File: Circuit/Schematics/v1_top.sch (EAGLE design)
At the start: 42 parts, among them IC1 LM2936MP-3.3, X2 16 Mhz, X3 16 Mhz

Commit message: Teensy board designed, redesigning system components board and making hardware components consistent
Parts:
- removed JP1: (no value), SparkFun-Connectors:M07
- added C10, C11, C12, C13, C14, C15, C16, C17, C18, C19, C20, C38, C39, C4, C40, C5, C6, C7, C8, C9: (no value), SparkFun-Capacitors:CAP0603-CAP
- added JP7: (no value), SparkFun-Connectors:M09
- added R1, R10, R11, R12, R13, R2, R5, R6: (no value), SparkFun-Resistors:RESISTOR0603-RES
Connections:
- new net SCL: JP7.9
- new net SDA: JP7.8
- net CE: now also JP7.3; no longer JP1.3
- net CSN: now also JP7.4; no longer JP1.4
- net MISO: now also JP7.6; no longer JP1.6
- net MOSI: now also JP7.5; no longer JP1.5
- net RX_W: now also JP7.1; no longer JP1.1
- net SCK: now also JP7.7; no longer JP1.7
- net TX_W: now also JP7.2; no longer JP1.2
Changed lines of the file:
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@@
 <part name="JP4" library="SparkFun-Connectors" deviceset="M02" device="LOCK"/>
 <part name="JP5" library="SparkFun-Connectors" deviceset="M02" device="LOCK"/>
-<part name="JP1" library="SparkFun-Connectors" deviceset="M07" device=""/>
 <part name="X3" library="crystals" deviceset="TXC-8Y" device="" value="16 Mhz"/>
 <part name="X2" library="crystals" deviceset="TXC-8Y" device="" value="16 Mhz"/>
 <part name="C1" library="SparkFun-Capacitors" deviceset="CAP" device="0402-CAP" value="1 uF"/>
 <part name="JP6" library="SparkFun-Connectors" deviceset="M02" device="LOCK"/>
+<part name="R1" library="SparkFun-Resistors" deviceset="RESISTOR" device="0603-RES"/>
+<part name="R2" library="SparkFun-Resistors" deviceset="RESISTOR" device="0603-RES"/>
+<part name="R5" library="SparkFun-Resistors" deviceset="RESISTOR" device="0603-RES"/>
+<part name="R6" library="SparkFun-Resistors" deviceset="RESISTOR" device="0603-RES"/>
+<part name="R10" library="SparkFun-Resistors" deviceset="RESISTOR" device="0603-RES"/>
+<part name="R11" library="SparkFun-Resistors" deviceset="RESISTOR" device="0603-RES"/>
+<part name="R12" library="SparkFun-Resistors" deviceset="RESISTOR" device="0603-RES"/>
+<part name="R13" library="SparkFun-Resistors" deviceset="RESISTOR" device="0603-RES"/>
+<part name="C4" library="SparkFun-Capacitors" deviceset="CAP" device="0603-CAP"/>
+<part name="C5" library="SparkFun-Capacitors" deviceset="CAP" device="0603-CAP"/>
+<part name="C6" library="SparkFun-Capacitors" deviceset="CAP" device="0603-CAP"/>
+<part name="C7" library="SparkFun-Capacitors" deviceset="CAP" device="0603-CAP"/>
+<part name="C8" library="SparkFun-Capacitors" deviceset="CAP" device="0603-CAP"/>
+<part name="C9" library="SparkFun-Capacitors" deviceset="CAP" device="0603-CAP"/>
+<part name="C10" library="SparkFun-Capacitors" deviceset="CAP" device="0603-CAP"/>
+<part name="C11" library="SparkFun-Capacitors" deviceset="CAP" device="0603-CAP"/>
+<part name="C12" library="SparkFun-Capacitors" deviceset="CAP" device="0603-CAP"/>
+<part name="C13" library="SparkFun-Capacitors" deviceset="CAP" device="0603-CAP"/>
+<part name="C14" library="SparkFun-Capacitors" deviceset="CAP" device="0603-CAP"/>
+<part name="C15" library="SparkFun-Capacitors" deviceset="CAP" device="0603-CAP"/>
+<part name="C16" library="SparkFun-Capacitors" deviceset="CAP" device="0603-CAP"/>
+<part name="C17" library="SparkFun-Capacitors" deviceset="CAP" device="0603-CAP"/>
+<part name="C18" library="SparkFun-Capacitors" deviceset="CAP" device="0603-CAP"/>
+<part name="C19" library="SparkFun-Capacitors" deviceset="CAP" device="0603-CAP"/>
+<part name="C20" library="SparkFun-Capacitors" deviceset="CAP" device="0603-CAP"/>
+<part name="C38" library="SparkFun-Capacitors" deviceset="CAP" device="0603-CAP"/>
+<part name="C39" library="SparkFun-Capacitors" deviceset="CAP" device="0603-CAP"/>
+<part name="C40" library="SparkFun-Capacitors" deviceset="CAP" device="0603-CAP"/>
+<part name="JP7" library="SparkFun-Connectors" deviceset="M09" device=""/>
 </parts>
 <sheets>
@@
 <instance part="JP4" gate="G$1" x="193.04" y="129.54" rot="R180"/>
 <instance part="JP5" gate="G$1" x="208.28" y="129.54" rot="R180"/>
-<instance part="JP1" gate="G$1" x="231.14" y="132.08" rot="R180"/>
 <instance part="X3" gate="G$1" x="60.96" y="104.14" rot="R90"/>
 <instance part="X2" gate="G$1" x="137.16" y="12.7"/>
 <instance part="C1" gate="G$1" x="93.98" y="111.76"/>
 <instance part="JP6" gate="G$1" x="203.2" y="109.22" rot="R180"/>
+<instance part="R1" gate="G$1" x="20.32" y="99.06"/>
+<instance part="R2" gate="G$1" x="55.88" y="2.54"/>
+<instance part="R5" gate="G$1" x="96.52" y="22.86"/>
+<instance part="R6" gate="G$1" x="152.4" y="22.86"/>
+<instance part="R10" gate="G$1" x="144.78" y="86.36"/>
+<instance part="R11" gate="G$1" x="205.74" y="22.86"/>
+<instance part="R12" gate="G$1" x="205.74" y="15.24"/>
+<instance part="R13" gate="G$1" x="205.74" y="7.62"/>
+<instance part="C4" gate="G$1" x="-2.54" y="76.2"/>
+<instance part="C5" gate="G$1" x="76.2" y="142.24"/>
+<instance part="C6" gate="G$1" x="73.66" y="116.84"/>
+<instance part="C7" gate="G$1" x="78.74" y="91.44"/>
+<instance part="C8" gate="G$1" x="93.98" y="99.06"/>
+<instance part="C9" gate="G$1" x="101.6" y="99.06"/>
+<instance part="C10" gate="G$1" x="129.54" y="99.06"/>
+<instance part="C11" gate="G$1" x="116.84" y="86.36"/>
+<instance part="C12" gate="G$1" x="137.16" y="99.06"/>
+<instance part="C13" gate="G$1" x="144.78" y="99.06"/>
+<instance part="C14" gate="G$1" x="149.86" y="99.06"/>
+<instance part="C15" gate="G$1" x="154.94" y="99.06"/>
+<instance part="C16" gate="G$1" x="160.02" y="99.06"/>
+<instance part="C17" gate="G$1" x="165.1" y="99.06"/>
+<instance part="C18" gate="G$1" x="180.34" y="76.2"/>
+<instance part="C19" gate="G$1" x="198.12" y="55.88"/>
+<instance part="C20" gate="G$1" x="160.02" y="25.4"/>
+<instance part="C38" gate="G$1" x="170.18" y="25.4"/>
+<instance part="C39" gate="G$1" x="132.08" y="-7.62"/>
+<instance part="C40" gate="G$1" x="142.24" y="-7.62"/>
+<instance part="JP7" gate="G$1" x="236.22" y="99.06" rot="R180"/>
 </instances>
 <busses>
@@
 </segment>
 <segment>
-<pinref part="JP1" gate="G$1" pin="2"/>
-<wire x1="226.06" y1="134.62" x2="223.52" y2="134.62" width="0.1524" layer="91"/>
+<pinref part="JP7" gate="G$1" pin="2"/>
+<wire x1="226.06" y1="106.68" x2="223.52" y2="106.68" width="0.1524" layer="91"/>
 </segment>
 </net>
@@
 </segment>
 <segment>
-<pinref part="JP1" gate="G$1" pin="1"/>
-<wire x1="226.06" y1="137.16" x2="223.52" y2="137.16" width="0.1524" layer="91"/>
+<pinref part="JP7" gate="G$1" pin="1"/>
+<wire x1="226.06" y1="109.22" x2="223.52" y2="109.22" width="0.1524" layer="91"/>
 </segment>
 </net>
@@
 </segment>
 <segment>
-<pinref part="JP1" gate="G$1" pin="3"/>
-<wire x1="226.06" y1="132.08" x2="223.52" y2="132.08" width="0.1524" layer="91"/>
+<pinref part="JP7" gate="G$1" pin="3"/>
+<wire x1="226.06" y1="104.14" x2="223.52" y2="104.14" width="0.1524" layer="91"/>
 </segment>
 </net>
@@
 </segment>
 <segment>
-<pinref part="JP1" gate="G$1" pin="4"/>
-<wire x1="226.06" y1="129.54" x2="223.52" y2="129.54" width="0.1524" layer="91"/>
+<pinref part="JP7" gate="G$1" pin="4"/>
+<wire x1="226.06" y1="101.6" x2="223.52" y2="101.6" width="0.1524" layer="91"/>
 </segment>
 </net>
@@
 </segment>
 <segment>
-<pinref part="JP1" gate="G$1" pin="7"/>
-<wire x1="226.06" y1="121.92" x2="223.52" y2="121.92" width="0.1524" layer="91"/>
+<pinref part="JP7" gate="G$1" pin="7"/>
+<wire x1="226.06" y1="93.98" x2="223.52" y2="93.98" width="0.1524" layer="91"/>
 </segment>
 </net>
@@
 </segment>
 <segment>
-<pinref part="JP1" gate="G$1" pin="5"/>
-<wire x1="226.06" y1="127" x2="223.52" y2="127" width="0.1524" layer="91"/>
+<pinref part="JP7" gate="G$1" pin="5"/>
+<wire x1="226.06" y1="99.06" x2="223.52" y2="99.06" width="0.1524" layer="91"/>
 </segment>
 </net>
@@
 </segment>
 <segment>
-<pinref part="JP1" gate="G$1" pin="6"/>
-<wire x1="226.06" y1="124.46" x2="223.52" y2="124.46" width="0.1524" layer="91"/>
+<pinref part="JP7" gate="G$1" pin="6"/>
+<wire x1="226.06" y1="96.52" x2="223.52" y2="96.52" width="0.1524" layer="91"/>
 </segment>
 </net>
@@
 </segment>
 </net>
+<net name="SDA" class="0">
+<segment>
+<pinref part="JP7" gate="G$1" pin="8"/>
+<wire x1="226.06" y1="91.44" x2="223.52" y2="91.44" width="0.1524" layer="91"/>
+</segment>
+</net>
+<net name="SCL" class="0">
+<segment>
+<pinref part="JP7" gate="G$1" pin="9"/>
+<wire x1="226.06" y1="88.9" x2="223.52" y2="88.9" width="0.1524" layer="91"/>
+</segment>
+</net>

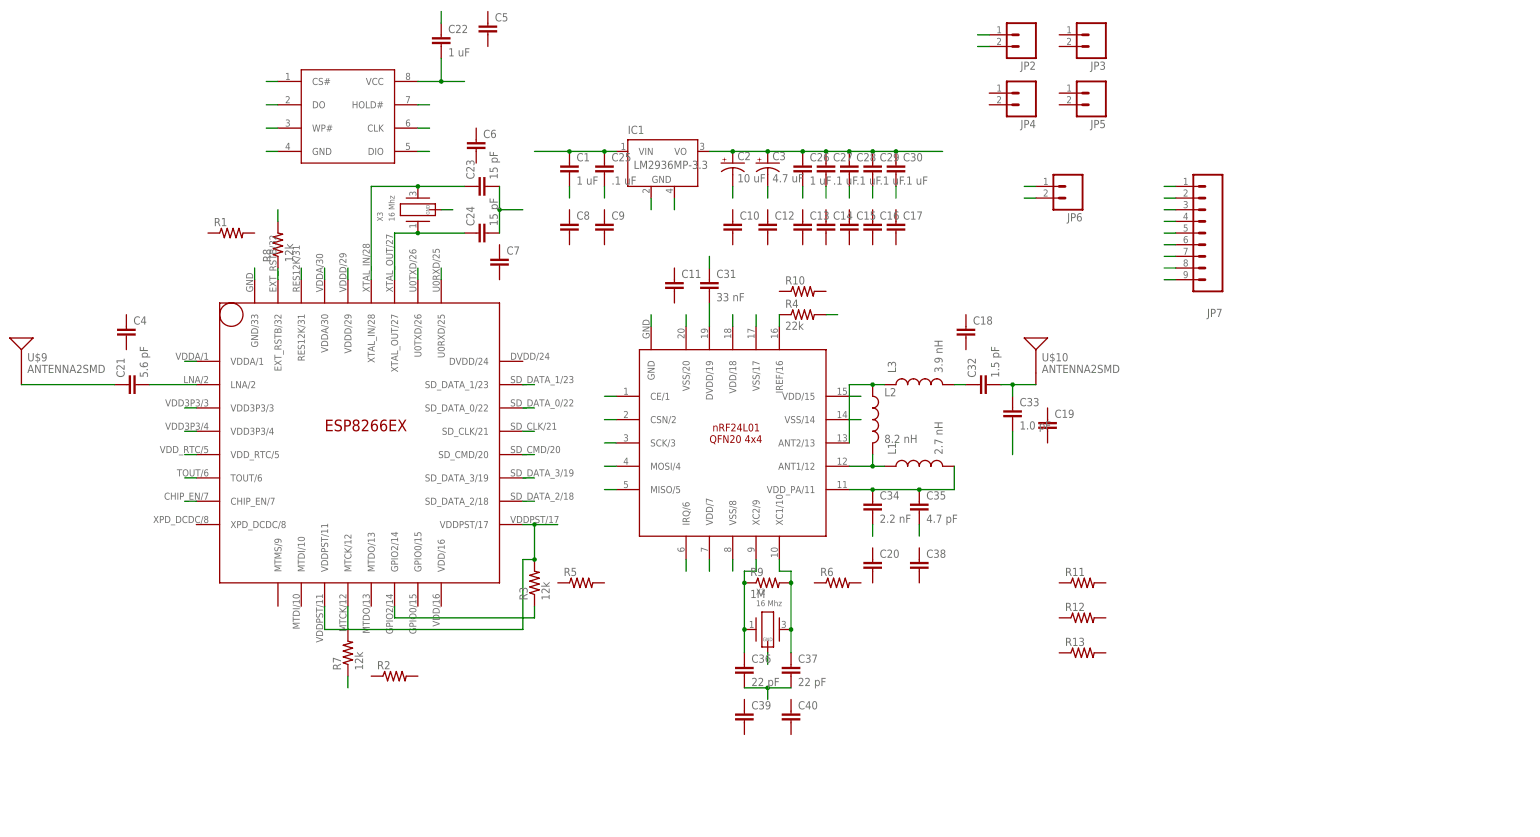
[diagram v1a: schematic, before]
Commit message: System components board almost done. Final tweaking
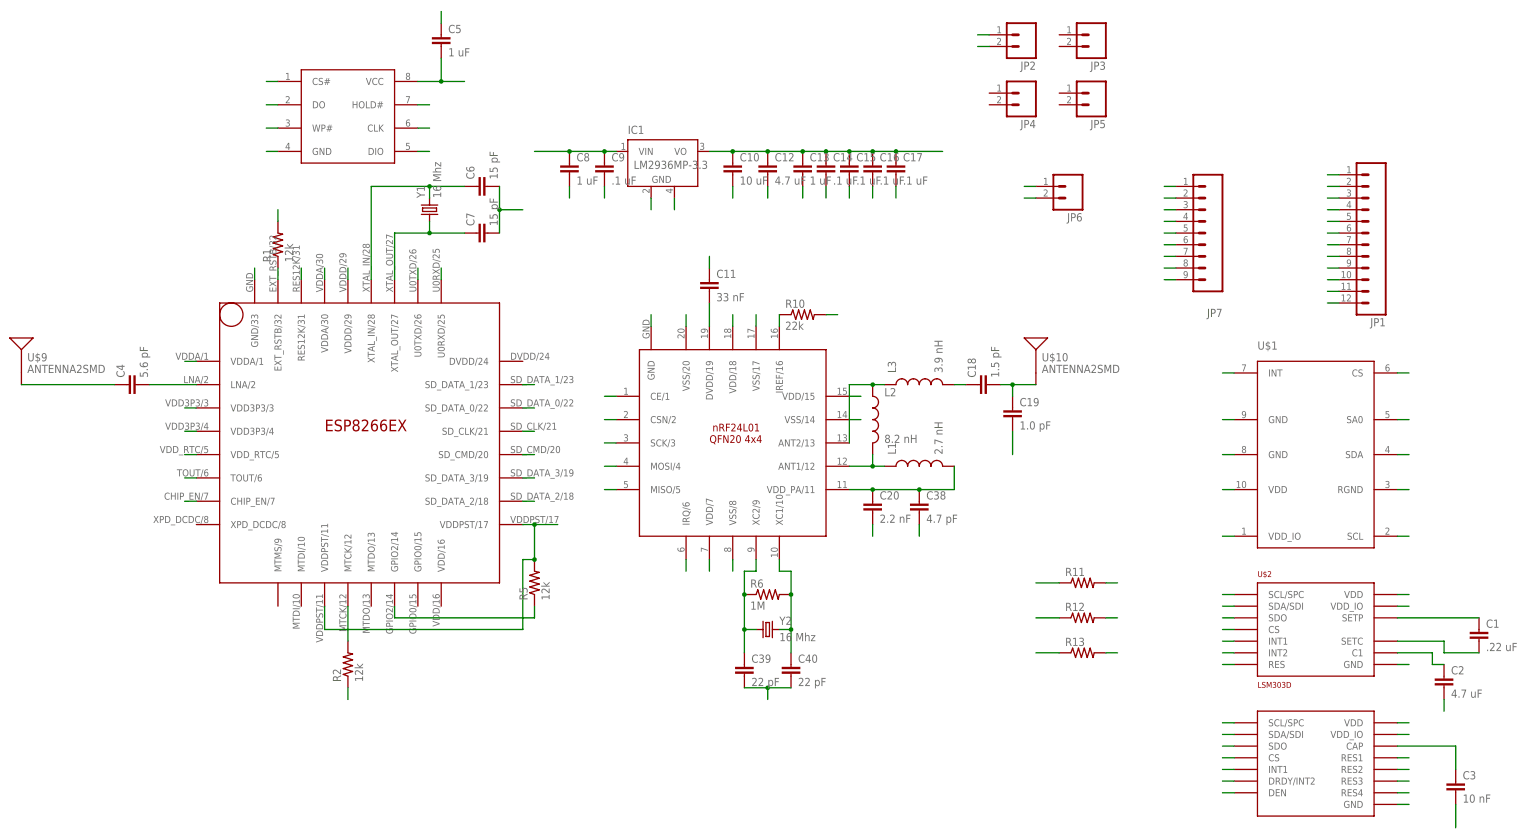
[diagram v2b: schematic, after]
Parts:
- removed C21: 5.6 pF, SparkFun-Capacitors:CAP0402-CAP
- removed C22, C26: 1 uF, SparkFun-Capacitors:CAP0402-CAP
- removed C23, C24: 15 pF, SparkFun-Capacitors:CAP0402-CAP
- removed C25, C27, C28, C29, C30: .1 uF, SparkFun-Capacitors:CAP0402-CAP
- removed C31: 33 nF, SparkFun-Capacitors:CAP0402-CAP
- removed C32: 1.5 pF, SparkFun-Capacitors:CAP0402-CAP
- removed C33: 1.0 pF, SparkFun-Capacitors:CAP0402-CAP
- removed C34: 2.2 nF, SparkFun-Capacitors:CAP0402-CAP
- removed C35: 4.7 pF, SparkFun-Capacitors:CAP0402-CAP
- removed C36, C37: 22 pF, SparkFun-Capacitors:CAP0402-CAP
- removed R3, R7, R8: 12k, SparkFun-Resistors:RESISTOR0402
- removed R4: 22k, SparkFun-Resistors:RESISTOR0402
- removed R9: 1M, SparkFun-Resistors:RESISTOR0402
- removed X2, X3: 16 Mhz, crystals:TXC-8Y
- added JP1: (no value), SparkFun-Connectors:M12PTH
- added U$1: LPS25H, chips:LPS25H
- added U$2: LSM303D, st:LSM303D
- added U$3: L3GD20H, st:L3GD20H
- added Y1, Y2: 16 Mhz, SparkFun-FreqCtrl:CRYSTAL5X3
- C1: value 1 uF -> .22 uF; device SparkFun-Capacitors:CAP0402-CAP -> SparkFun-Capacitors:CAP0603-CAP
- C10: value (none) -> 10 uF
- C11: value (none) -> 33 nF
- C12: value (none) -> 4.7 uF
- C13, C5, C8: value (none) -> 1 uF
- C14, C15, C16, C17, C9: value (none) -> .1 uF
- C18: value (none) -> 1.5 pF
- C19: value (none) -> 1.0 pF
- C2: value 10 uF -> 4.7 uF; device SparkFun-Capacitors:CAP_POL1206 -> SparkFun-Capacitors:CAP0603-CAP
- C20: value (none) -> 2.2 nF
- C3: value 4.7 uF -> 10 nF; device SparkFun-Capacitors:CAP_POL1206 -> SparkFun-Capacitors:CAP0603-CAP
- C38: value (none) -> 4.7 pF
- C39, C40: value (none) -> 22 pF
- C4: value (none) -> 5.6 pF
- C6, C7: value (none) -> 15 pF
- R1, R2, R5: value (none) -> 12k
- R10: value (none) -> 22k
- R6: value (none) -> 1M
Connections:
- removed net N$12: R7.2, WIFI.MTCK/12
- new net N$14: U$1.INT
- new net N$3: R2.2, WIFI.MTCK/12
- new net N$35: U$2.INT1
- new net N$36: U$2.INT2
- new net N$42: C1.2, U$2.SETC
- new net N$43: C2.1, U$2.C1
- new net N$49: U$3.INT1
- new net N$50: U$3.DRDY/INT2
- new net N$54: C3.1, U$3.CAP
- new net N$58: U$3.RES4
- new net SDO: R13.2, U$1.SA0, U$2.SDO, U$3.SDO
- new net SETP: C1.1, U$2.SETP
- net GND: now also C10.2, C11.1, C12.2, C13.2, C14.2, C15.2, C16.2, C17.2, C19.2, C2.2, C20.2, C3.2, C38.2, C39.2, C40.2, C5.1, C6.2, C7.2, C8.2, C9.2, JP1.1, JP1.2, JP1.3, JP1.4, JP1.5, JP1.6, R1.2, R10.2, R2.1, U$1.GND@1, U$1.GND@2, U$1.RGND, U$2.GND, U$2.RES, U$3.DEN, U$3.GND, U$3.RES1, U$3.RES2, U$3.RES3; no longer C1.2, C2.-, C22.1, C23.2, C24.2, C25.2, C26.2, C27.2, C28.2, C29.2, C3.-, C30.2, C31.1, C33.2, C34.2, C35.2, C36.2, C37.2, R4.2, R7.1, R8.2, X2.GND, X3.GND
- net N$1: now also C4.1; no longer C21.1
- net N$10: now also C18.2, C19.1; no longer C32.2, C33.1
- net N$13: now also C4.2; no longer C21.2
- net N$16: now also C39.1, R6.1, Y2.1; no longer C36.1, R9.1, X2.1
- net N$17: now also C40.1, R6.2, Y2.2; no longer C37.1, R9.2, X2.2
- net N$18: now also C20.1, C38.1; no longer C34.1, C35.1
- net N$2: now also R5.1; no longer R3.1
- net N$24: now also R10.1; no longer R4.1
- net N$28: now also C11.2; no longer C31.2
- net N$6: now also C18.1; no longer C32.1
- net RST: now also R1.1; no longer R8.1
- net SCL: now also R12.2, U$1.SCL, U$2.SCL/SPC, U$3.SCL/SPC
- net SDA: now also R11.2, U$1.SDA, U$2.SDA/SDI, U$3.SDA/SDI
- net VDD: now also C10.1, C12.1, C13.1, C14.1, C15.1, C16.1, C17.1, C5.2, JP1.10, JP1.11, JP1.12, JP1.7, JP1.8, JP1.9, R11.1, R12.1, R13.1, R5.2, U$1.CS, U$1.VDD, U$1.VDD_IO, U$2.CS, U$2.VDD, U$2.VDD_IO, U$3.CS, U$3.VDD, U$3.VDD_IO; no longer C2.+, C22.2, C26.1, C27.1, C28.1, C29.1, C3.+, C30.1, R3.2
- net VRAW: now also C8.1, C9.1; no longer C1.1, C25.1
- net XTAL_IN: now also C6.1, Y1.2; no longer C23.1, X3.2
- net XTAL_OUT: now also C7.1, Y1.1; no longer C24.1, X3.1
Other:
- moved on the sheet: C1, C10, C11, C12, C13, C14, C15, C16, C17, C18, C19, C20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
